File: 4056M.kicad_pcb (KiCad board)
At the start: 2 copper layers, 21.1 x 16 mm, 25 parts, among them J1 VBUS, J2 GND, J3 Conn_01x02_MountingPin, J4 3V3, J5 state, J6 measure, Q1 3401, Q2 8050, Q3 3401, U1 TC4056A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

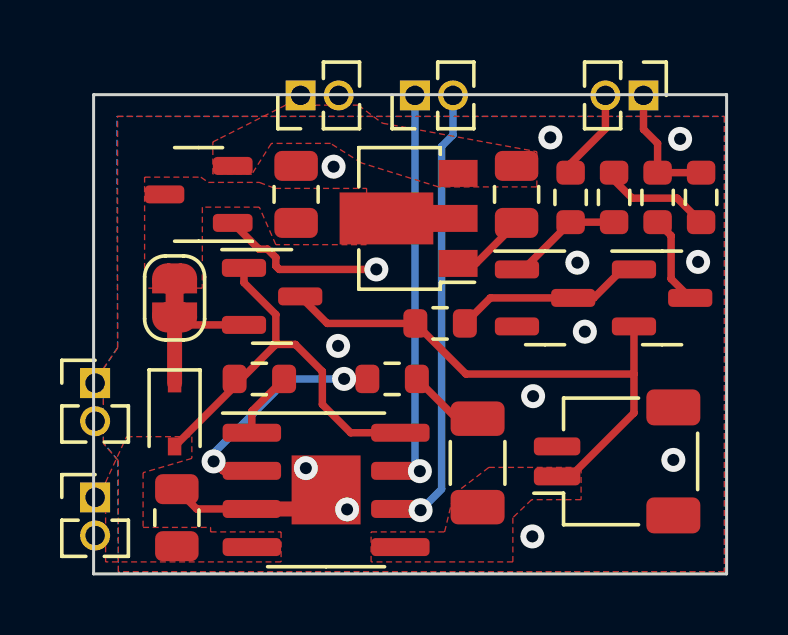
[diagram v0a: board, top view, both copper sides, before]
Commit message: 电池座PIN1应该为GND
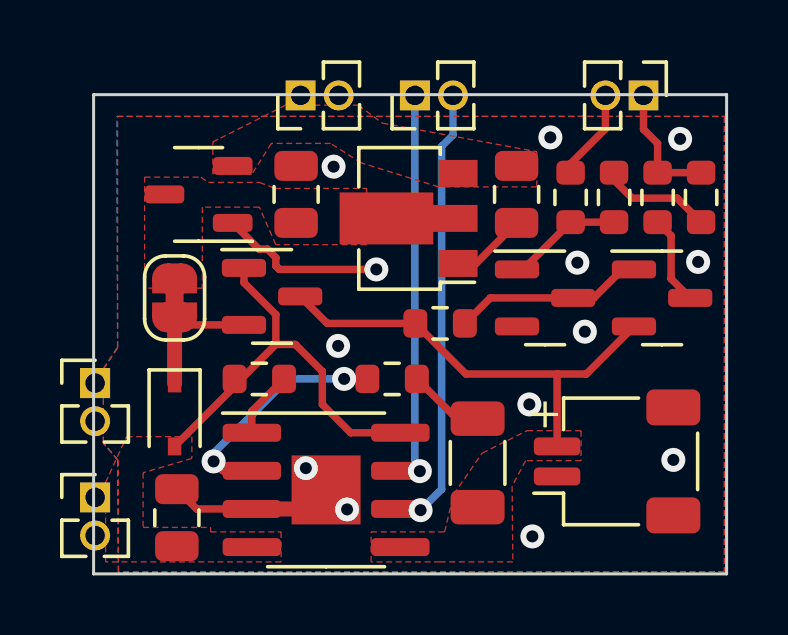
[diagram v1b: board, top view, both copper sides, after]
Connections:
- C1 pad 1: GND -> -BATT
- C2 pad 1: GND -> -BATT
- C3 pad 1: GND -> -BATT
- C4 pad 1: GND -> -BATT
- J2 pad 1: GND -> -BATT
- J2 pad 2: GND -> -BATT
- J3 pad 1: +BATT -> -BATT
- J3 pad 2: GND -> +BATT
- J3 pad MP: GND -> -BATT
- Q2 pad 2: GND -> -BATT
- R1 pad 1: GND -> -BATT
- R2 pad 1: GND -> -BATT
- R5 pad 2: GND -> -BATT
- R8 pad 2: GND -> -BATT
- U1 pad 1: GND -> -BATT
- U1 pad 3: GND -> -BATT
- U1 pad 9: GND -> -BATT
- U2 pad 1: GND -> -BATT
- U3 pad 1: GND -> -BATT
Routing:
- net -BATT: track 0.00 -> 22.6 mm, vias 0 -> 13
- net GND: track 22.2 -> 0.00 mm, vias 13 -> 0
- net +BATT: track 18.5 -> 15.3 mm
- added copper zone on B.Cu, net -BATT
- added copper zone on F.Cu, net -BATT
- removed copper zone on B.Cu, net GND
- removed copper zone on F.Cu, net GND
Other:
- board text added: "+"

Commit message: New version
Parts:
- removed Q2: 8050, Package_TO_SOT_SMD:SOT-23
- removed Q3: 3401, Package_TO_SOT_SMD:SOT-23
- removed R7: 4.7K, Resistor_SMD:R_0603_1608Metric
- removed R8: 1K, Resistor_SMD:R_0603_1608Metric
- added C5: 1uF, Capacitor_SMD:C_0603_1608Metric, F.Cu at (120.3, 84.1)
- added C6: 1uF, Capacitor_SMD:C_0603_1608Metric, F.Cu at (124.9, 84.1)
- added U4: CW2015, Package_DFN_QFN:TDFN-8-1EP_3x2mm_P0.5mm_EP1.4x1.4mm, F.Cu at (121.3, 80.3)
- C2: footprint Capacitor_SMD:C_1206_3216Metric -> Capacitor_SMD:C_0603_1608Metric
- J6: value measure -> Conn_01x04; footprint Connector_PinHeader_1.27mm:PinHeader_1x02_P1.27mm_Vertical -> Connector_PinHeader_1.27mm:PinHeader_1x04_P1.27mm_Vertical
- R2: footprint Resistor_SMD:R_0603_1608Metric -> Resistor_SMD:R_0402_1005Metric
- R4: value 1K -> 470R
- R5: value 100K -> 100R
- R6: value 10K -> 4.7K
- U1: value TC4056A -> TP4057; footprint Package_SO:HSOP-8-1EP_3.9x4.9mm_P1.27mm_EP2.3x2.3mm -> Package_TO_SOT_SMD:SOT-23-6
- moved C4 10.9 mm to (113.2, 78.4), turned to 0 degrees
- moved R1 7.28 mm to (115.3, 90.6)
- moved J5 7.00 mm to (126.2, 80.0), turned to 0 degrees
- moved R4 6.59 mm to (121.8, 84.1), turned to 90 degrees
- moved R5 6.54 mm to (123.3, 84.1)
- moved J3 4.71 mm to (122.9, 88.5)
- moved C2 4.08 mm to (118.8, 88.2), turned to 90 degrees
- moved J4 4.05 mm to (112.9, 75.5)
- moved J6 4.02 mm to (124.4, 75.5)
- moved U2 3.98 mm to (117.5, 79.4), turned to -90 degrees
- moved C3 3.91 mm to (113.2, 80.4), turned to 0 degrees
- moved R6 3.90 mm to (123.4, 79.7), turned to 90 degrees
- moved U3 3.07 mm to (117.5, 80.0), turned to -90 degrees
- moved Q1 2.54 mm to (116.9, 84.6), turned to 180 degrees
- moved U1 1.97 mm to (115.9, 88.1), turned to 180 degrees
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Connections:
- J5 pad 1: /CHRG -> /STDBY
- J5 pad 2: /STDBY -> /CHRG
- J6 pad 1: /ADC -> /PS
- J6 pad 2: /IO -> /ALRT
- R4 pad 1: /IO -> +BATT
- R4 pad 2: Net-(Q2-Pad1) -> Net-(C5-Pad2)
- R5 pad 1: Net-(Q2-Pad1) -> +BATT
- R5 pad 2: -BATT -> Net-(C6-Pad1)
- R6 pad 1: +BATT -> /PS
- R6 pad 2: Net-(Q2-Pad3) -> /ALRT
- U1 pad 1: -BATT -> /CHRG
- U1 pad 2: Net-(R1-Pad2) -> -BATT
- U1 pad 3: -BATT -> +BATT
- U1 pad 5: +BATT -> /STDBY
- U1 pad 6: /STDBY -> Net-(R1-Pad2)
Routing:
- net -BATT: track 22.6 -> 0.00 mm, vias 13 -> 21
- net VBUS: track 13.9 -> 0.00 mm
- net +BATT: track 15.3 -> 5.46 mm
- net Net-(Q2-Pad3): track 6.38 -> 0.00 mm
- net Net-(R1-Pad2): track 7.83 -> 1.66 mm, vias 2 -> 0
- net /PS: track 0.00 -> 5.26 mm
- net Net-(D1-Pad1): track 4.62 -> 0.00 mm
- net /ALRT: track 0.00 -> 4.25 mm
- net Net-(C6-Pad1): track 0.00 -> 4.24 mm
- net /ADC: track 4.22 -> 0.00 mm
- net Net-(Q2-Pad1): track 3.89 -> 0.00 mm
- net /SCL: track 0.00 -> 3.53 mm
- net /SDA: track 0.00 -> 3.21 mm
- net Net-(C5-Pad2): track 0.00 -> 3.08 mm
- net /IO: track 3.06 -> 0.00 mm
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- added copper zone on F.Cu, net Net-(D1-Pad1)
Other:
- board size 21.1 x 16 mm -> 16.1 x 16 mm
- board text added: "-"
- board text added: "Power Module"
